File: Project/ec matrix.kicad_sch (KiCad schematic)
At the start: 46 parts

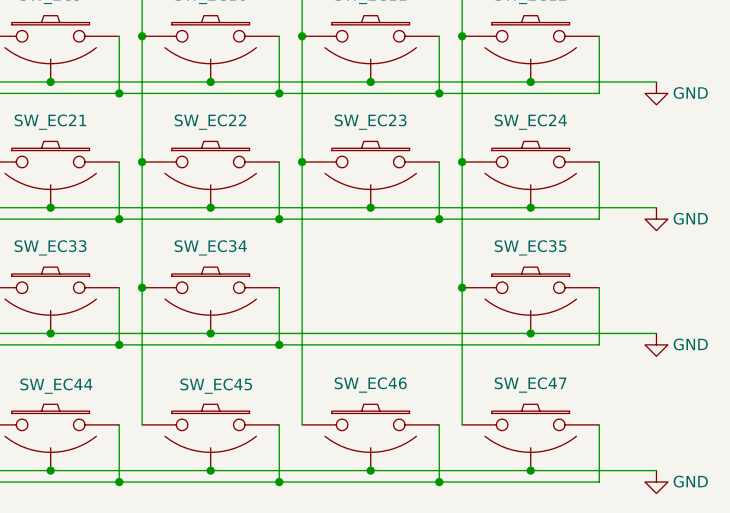
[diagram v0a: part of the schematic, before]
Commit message: redesign after missing switch
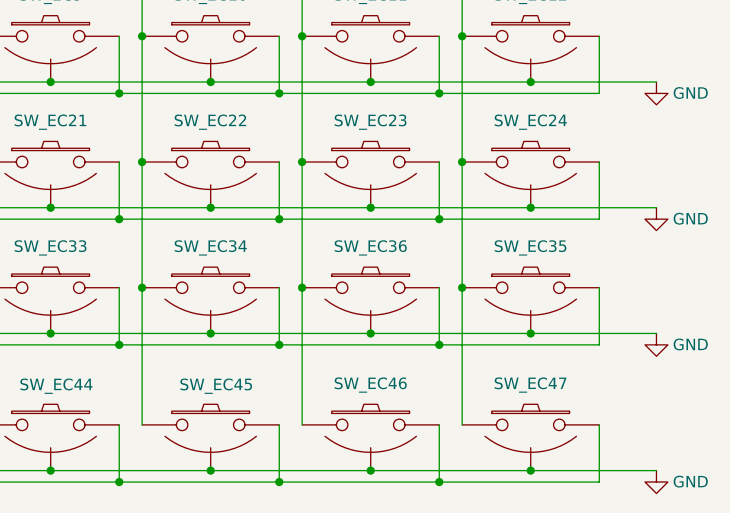
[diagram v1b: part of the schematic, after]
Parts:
- added SW_EC36: Topre, cipulot_parts:ecs_pad_1U_no_ring, symbol cipulot_parts:EC_SW
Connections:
- net COL10: now also SW_EC36.1
- net GND: now also SW_EC36.3 (SG)
- net ROW2: now also SW_EC36.2
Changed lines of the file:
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@@
   (junction (at 147.955 67.945) (diameter 0) (color 0 0 0 0)
   )
+  (junction (at 229.235 66.675) (diameter 0) (color 0 0 0 0)
+  )
   (junction (at 94.615 83.185) (diameter 0) (color 0 0 0 0)
   )
@@
   (junction (at 59.055 40.005) (diameter 0) (color 0 0 0 0)
   )
+  (junction (at 236.855 67.945) (diameter 0) (color 0 0 0 0)
+  )
   (junction (at 59.055 53.975) (diameter 0) (color 0 0 0 0)
   )
@@
   (junction (at 211.455 52.705) (diameter 0) (color 0 0 0 0)
   )
+  (junction (at 221.615 61.595) (diameter 0) (color 0 0 0 0)
+  )
   (junction (at 112.395 83.185) (diameter 0) (color 0 0 0 0)
   )
@@
     (stroke (width 0) (type default))
   )
-  (wire (pts (xy 211.455 66.675) (xy 247.015 66.675))
+  (wire (pts (xy 211.455 66.675) (xy 229.235 66.675))
     (stroke (width 0) (type default))
   )
@@
     (stroke (width 0) (type default))
   )
+  (wire (pts (xy 229.235 66.675) (xy 247.015 66.675))
+    (stroke (width 0) (type default))
+  )
   (wire (pts (xy 130.175 83.185) (xy 147.955 83.185))
     (stroke (width 0) (type default))
@@
     (stroke (width 0) (type default))
   )
+  (wire (pts (xy 236.855 61.595) (xy 236.855 67.945))
+    (stroke (width 0) (type default))
+  )
   (wire (pts (xy 239.395 47.625) (xy 239.395 61.595))
     (stroke (width 0) (type default))
@@
     (stroke (width 0) (type default))
   )
+  (wire (pts (xy 236.855 67.945) (xy 254.635 67.945))
+    (stroke (width 0) (type default))
+  )
   (wire (pts (xy 86.995 38.735) (xy 104.775 38.735))
     (stroke (width 0) (type default))
@@
     (stroke (width 0) (type default))
   )
-  (wire (pts (xy 219.075 67.945) (xy 254.635 67.945))
+  (wire (pts (xy 219.075 67.945) (xy 236.855 67.945))
     (stroke (width 0) (type default))
   )
@@
     (stroke (width 0) (type default))
   )
+  (wire (pts (xy 221.615 61.595) (xy 221.615 76.835))
+    (stroke (width 0) (type default))
+  )
   (wire (pts (xy 219.075 33.655) (xy 219.075 40.005))
     (stroke (width 0) (type default))
@@
     (stroke (width 0) (type default))
   )
-  (wire (pts (xy 221.615 47.625) (xy 221.615 76.835))
+  (wire (pts (xy 221.615 47.625) (xy 221.615 61.595))
     (stroke (width 0) (type default))
   )
@@
         )
       )
+    )
+  )
+  (symbol (lib_id "cipulot_parts:EC_SW") (at 229.235 61.595 0) (unit 1)
+    (in_bom yes) (on_board yes) (dnp no)
+    (property "Reference" "SW_EC36" (at 229.235 57.023 0)
+      (effects (font (size 1.27 1.27)))
+    )
+    (property "Value" "Topre" (at 229.235 57.785 0)
+      (effects (font (size 1.27 1.27)) hide)
+    )
+    (property "Footprint" "cipulot_parts:ecs_pad_1U_no_ring" (at 229.235 61.595 0)
+      (effects (font (size 1.27 1.27)) hide)
+    )
+    (property "Datasheet" "" (at 229.235 61.595 0)
+      (effects (font (size 1.27 1.27)))
+    )
+    (pin "1")
+    (pin "2")
+    (pin "3")
+    (instances
+      (project "oceanographer EC"
+        (path "/09508a56-789d-476d-953d-fdbb5c44fd9c/41c12397-a0ce-41dc-8ce2-3c576320707a"
+          (reference "SW_EC36") (unit 1)
+        )
+      )
+      (project "EC matrix"
+        (path "/5cff3ebd-5653-4200-a83d-5e749ea2bf15"
+          (reference "SW_EC35") (unit 1)
+        )
+      )
+      (project "forti EC"
+        (path "/f5e5948c-eeca-4160-a5f8-686f765d01ce/18429cf0-a58f-4ff2-8d01-5d33e3cc3dca"
+          (reference "SW_EC24") (unit 1)
+        )
+      )
